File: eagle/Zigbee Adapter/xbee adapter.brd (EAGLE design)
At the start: 41.6 x 38.6 mm, 15 parts, among them J3 POW_CONNECTMALE

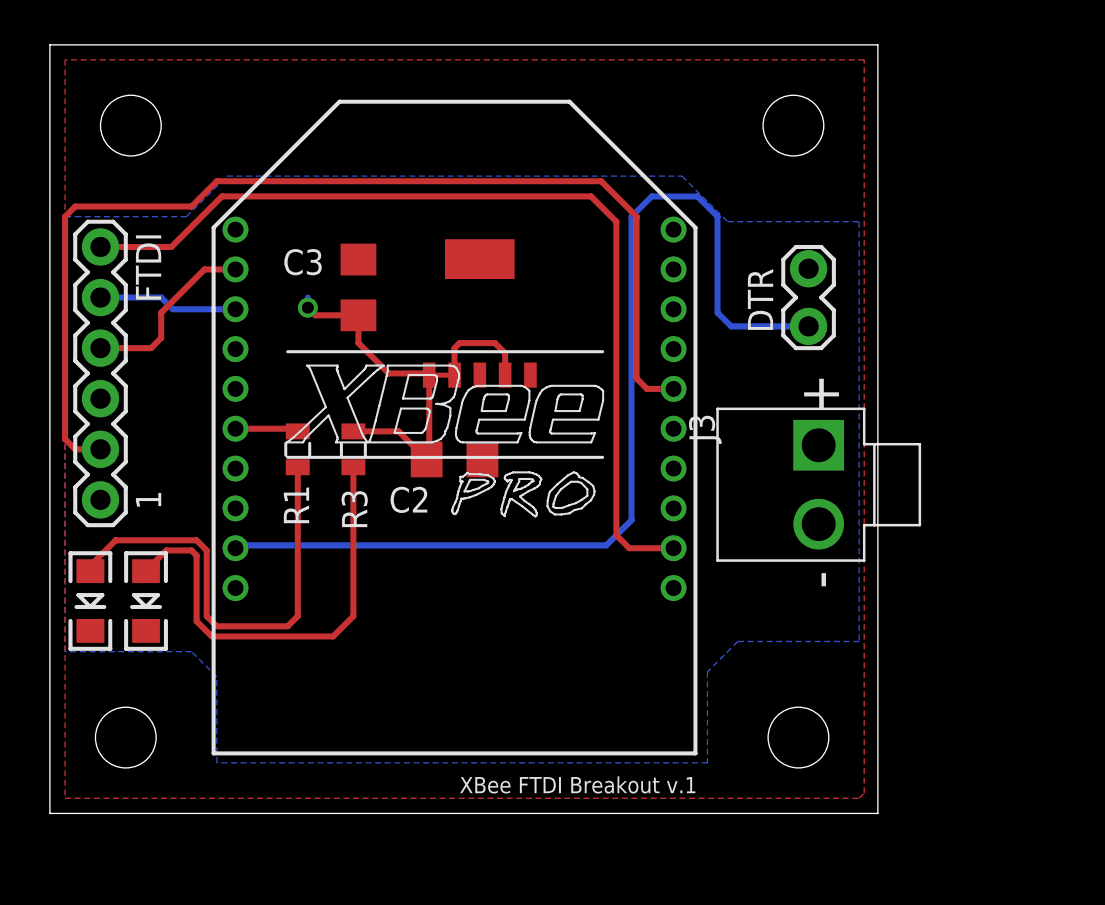
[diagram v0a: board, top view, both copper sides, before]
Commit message: New rs232 adapter for xbee.
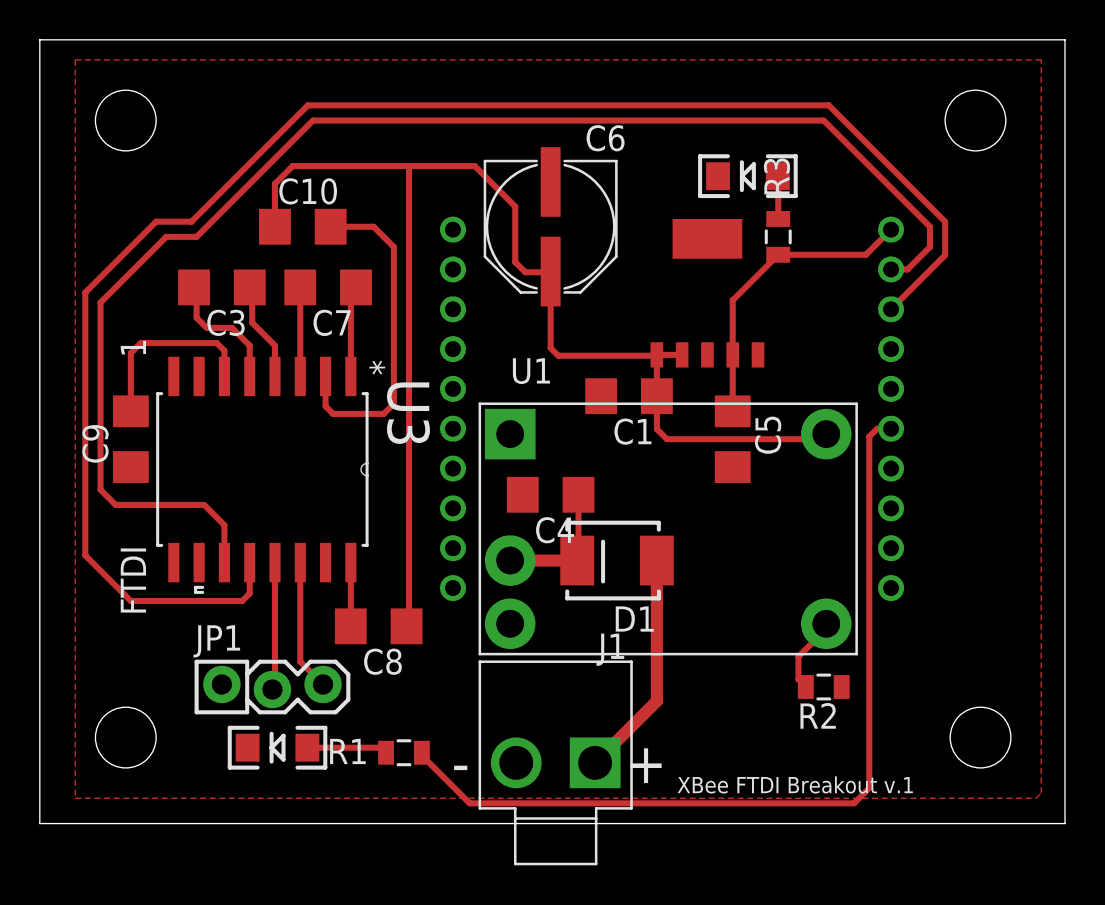
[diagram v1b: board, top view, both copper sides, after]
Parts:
- removed C2: 4.7 uF, ASL:1206
- removed J2: (no value), ASL:1X02_LOCK
- removed J3: POW_CONNECTMALE, ASL:SOCKET-MALE-3.96MM-2
- removed U$1: MCP1826, ASL:SOT223-5
- added C1: 4.7 uF, ASL:1206
- added C10, C7, C8, C9: (no value), ASL:1206
- added C4: 2.2uF, CMPE118lib:1206
- added C5: 1 uF, ASL:1206
- added C6: 100uF, CMPE118lib:CPOL_6.6
- added D1: DIODE-SCHOTTKY240A, CMPE118lib:SMA-DIODE-B240A
- added J1: POW_CONNECTMALE, CMPE118lib:SOCKET-MALE-3.96MM-2
- added R2: 21k, CMPE118lib:0805
- added U$2: MCP1826, ASL:SOT223-5
- added U1: PTN78000, ASL:PTN78000
- added U3: MAX232DW, Texas Instruments_By_element14_Batch_1:SOIC127P1030X265-16N
- C3: value 1 uF -> (none)
- JP1: value (none) -> M03LOCK; device ASL:1X06 -> ASL:1X03_LOCK
- moved LED2 37.0 mm to (35.1, 32.0), turned to 180 degrees
- moved R3 23.9 mm to (36.6, 29.0), turned to 270 degrees
- moved JP1 16.9 mm to (8.64, 6.35), turned to 0 degrees
- moved R1 16.1 mm to (17.8, 3.05), turned to 180 degrees
- moved LED1 11.9 mm to (11.4, 3.30), turned to 180 degrees
- moved XB1 10.9 mm to (31.2, 20.3), flipped to the bottom
- moved E$4 9.15 mm to (46.5, 34.8)
- moved E$3 9.14 mm to (46.7, 3.81)
- moved C3 6.86 mm to (8.64, 26.4), turned to 180 degrees
- moved E$1 0.36 mm to (3.81, 34.8)
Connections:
- removed net DIN: JP1.5, XB1.3
- removed net DOUT: JP1.4, XB1.2
- removed net N$3: JP1.3
- new net N$1: C3.2, U3.5
- new net N$10: C8.2, U3.16
- new net N$11: C9.2, U3.6
- new net N$12: C10.2, U3.2
- new net N$15: C3.1, U3.4
- new net N$16: C7.1, U3.1
- new net N$6: R2.2, U1.ADJ
- new net N$7: C7.2, U3.3
- new net N$8: C4.1, D1.C, U1.V_IN
- new net N$9: D1.A, J1.P$1
- new net RS232RX: JP1.2, U3.13
- new net RS232TX: JP1.3, U3.14
- new net RX: U3.12, XB1.3
- new net TX: U3.11, XB1.2
- new net VCC3V3: C5.1, R3.2, U$2.P$4, XB1.1
- net CTS: no longer JP1.6
- net DTR: no longer J2.1
- net GND: now also C1.2, C4.2, C5.2, C6.-, C9.1, J1.P$2, R2.1, U$2.P$3, U$2.P$6, U1.GND, U3.15; no longer C2.2, C3.2, J3.P$2, U$1.P$3, U$1.P$6
- net RTS: no longer JP1.2
- net VCC: now also C1.1, C10.1, C6.+, C8.1, U$2.P$1, U$2.P$2, U1.V_OUT; no longer C2.1, C3.1, J2.2, J3.P$1, R3.2, U$1.P$1, U$1.P$2, U$1.P$4, XB1.1
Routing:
- net RX: track 0.00 -> 79.1 mm
- net TX: track 0.00 -> 69.3 mm
- net RTS: track 53.5 -> 0.00 mm
- net DTR: track 50.6 -> 0.00 mm
- net CTS: track 46.4 -> 0.00 mm
- net VCC: track 24.0 -> 66.6 mm, vias 1 -> 0
- net N$2: track 3.18 -> 42.8 mm
- net N$5: track 22.5 -> 2.16 mm
- net N$4: track 22.6 -> 4.06 mm
- net N$12: track 0.00 -> 16.8 mm
- net VCC3V3: track 0.00 -> 15.0 mm
- net N$9: track 0.00 -> 11.4 mm
- net N$11: track 0.00 -> 9.28 mm
- net DOUT: track 9.16 -> 0.00 mm
- net DIN: track 7.02 -> 0.00 mm
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- removed copper zone on layer 16, net VCC
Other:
- board size 41.6 x 38.6 mm -> 51.5 x 39.4 mm
- board text removed: "DTR"

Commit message: New 1-Axis Test BLDC breakout for gluon stab
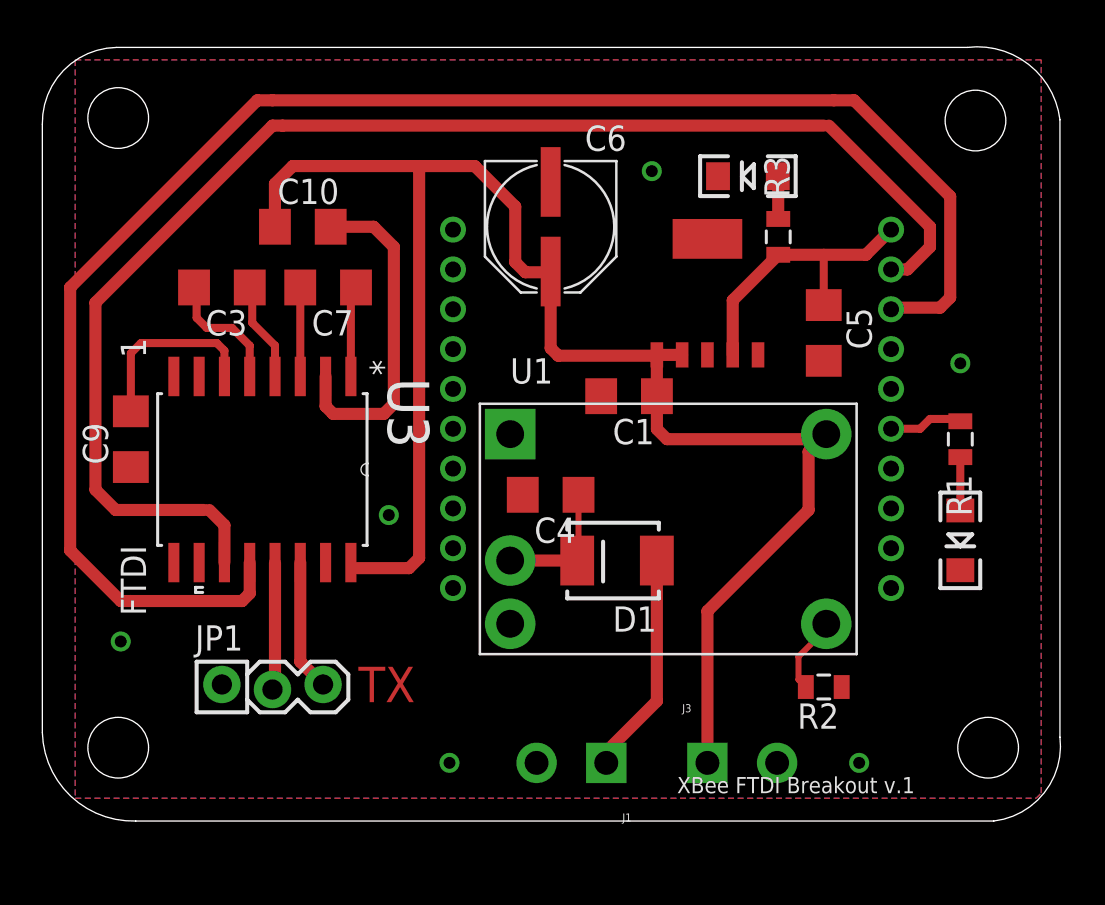
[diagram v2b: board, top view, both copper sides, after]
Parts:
- removed C8: (no value), ASL:1206
- removed E$1: (no value), ASL:STAND-OFF-TIGHT
- added E$5: (no value), ASL:STAND-OFF-TIGHT
- added J3: (no value), ASL:SCREWTERMINAL-3.5MM-2-NS
- J1: value POW_CONNECTMALE -> (none); device CMPE118lib:SOCKET-MALE-3.96MM-2 -> ASL:SCREWTERMINAL-3.5MM-2-NS
- moved LED1 35.8 mm to (45.7, 13.7), turned to 270 degrees
- moved R1 32.1 mm to (45.7, 18.8), turned to 270 degrees
- moved C5 7.03 mm to (38.9, 24.1)
- moved J1 2.54 mm to (27.9, 2.54)
- moved E$2 0.64 mm to (3.43, 3.30)
- moved E$3 0.64 mm to (47.1, 3.30)
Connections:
- removed net N$10: C8.2, U3.16
- net GND: now also J1.2, J3.2; no longer J1.P$2
- net N$9: now also J1.1; no longer J1.P$1
- net VCC: now also J3.1, U3.16; no longer C8.1
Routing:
- net N$2: track 42.8 -> 3.73 mm
- net VCC: track 66.6 -> 85.8 mm
- net RX: track 79.1 -> 83.4 mm
- net N$10: track 3.20 -> 0.00 mm
- net N$4: track 4.06 -> 2.68 mm
- added copper zone on layer 16, net GND
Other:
- board size 51.5 x 39.4 mm -> 51.1 x 38.9 mm
- board text added: "TX"
